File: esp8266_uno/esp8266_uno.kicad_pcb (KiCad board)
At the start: 2 copper layers, 68.5 x 53.5 mm, 126 parts, among them J1 Barrel_Jack, P1 USB, Q1 2N2222, Q2 2N2222, SW1 RESET, U1 ESP-12, U2 AMS1117-3.3, U3 CH340G, U4 ESP-13-WROOM-02, X1 12MHz

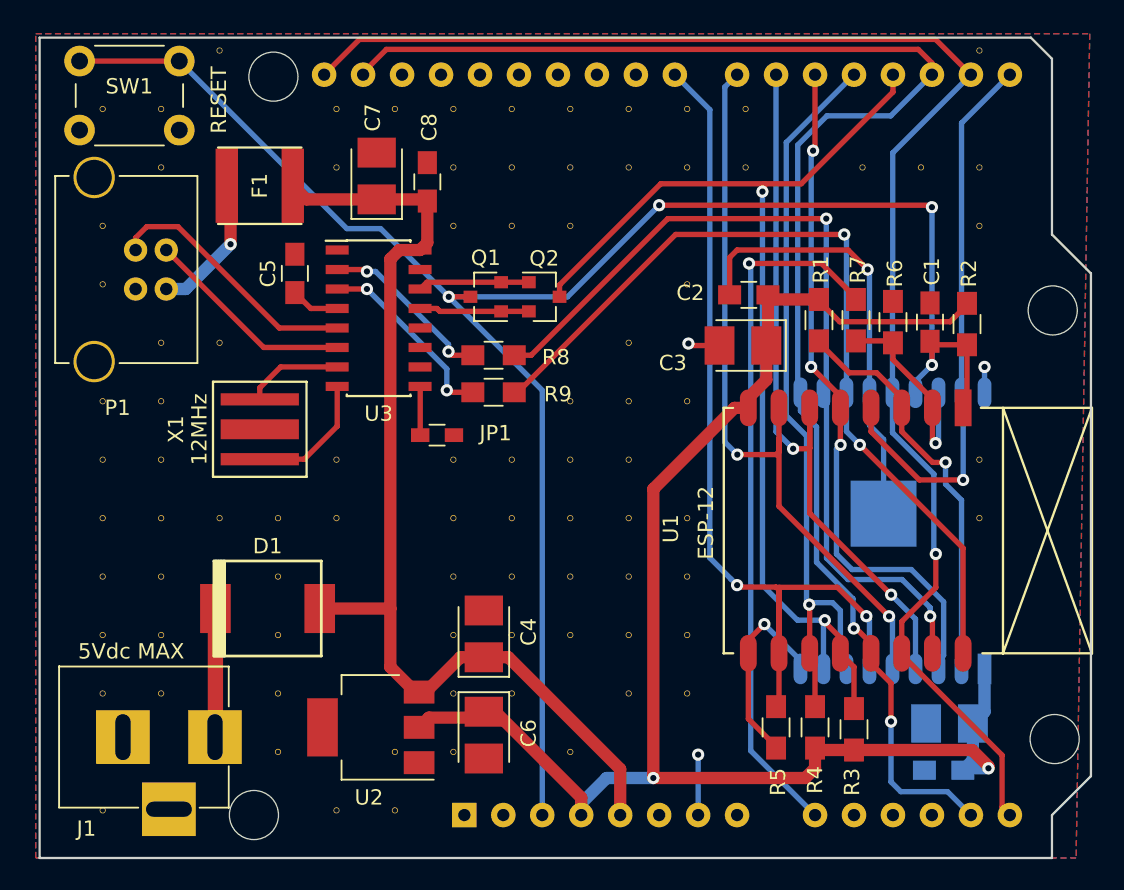
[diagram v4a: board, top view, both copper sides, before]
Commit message: added esp8266 in arduino uno format - hw design final touches
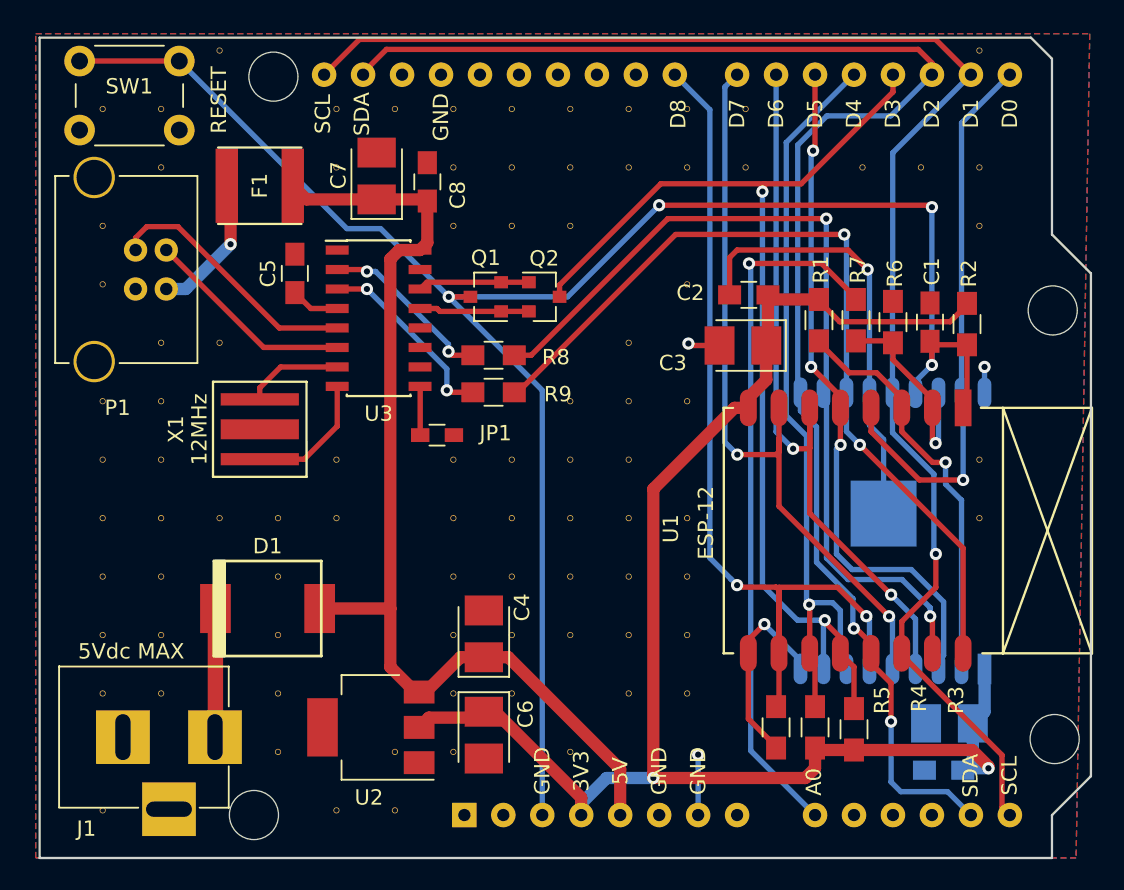
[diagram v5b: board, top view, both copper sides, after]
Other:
- board text added: "3V3"
- board text added: "5V"
- board text added: "A0"
- board text added: "D0"
- board text added: "D1"
- board text added: "D2"
- board text added: "D3"
- board text added: "D4"
- board text added: "D5"
- board text added: "D6"
- board text added: "D7"
- board text added: "D8"
- board text added: "GND"
- board text added: "SCL"
- board text added: "SDA"
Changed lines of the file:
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@@
   (general
     (thickness 1.6)
-    (drawings 56)
+    (drawings 96)
     (tracks 376)
     (zones 0)
@@
     (tags "capacitor 0805")
     (attr smd)
-    (fp_text reference C8 (at -3.556 -0.127 270) (layer F.SilkS)
+    (fp_text reference C8 (at 0.8636 -1.9812 270) (layer F.SilkS)
       (effects (font (size 1 1) (thickness 0.15)))
     )
@@
     (tags "resistor 0805")
     (attr smd)
-    (fp_text reference R3 (at 3.429 0.127 270) (layer F.SilkS)
+    (fp_text reference R3 (at -1.905 -6.6548 270) (layer F.SilkS)
       (effects (font (size 1 1) (thickness 0.15)))
     )
@@
     (tags "resistor 0805")
     (attr smd)
-    (fp_text reference R4 (at 3.429 0 270) (layer F.SilkS)
+    (fp_text reference R4 (at -1.905 -6.7818 270) (layer F.SilkS)
       (effects (font (size 1 1) (thickness 0.15)))
     )
@@
     (tags "resistor 0805")
     (attr smd)
-    (fp_text reference R5 (at 3.556 -0.127 270) (layer F.SilkS)
+    (fp_text reference R5 (at -1.778 -6.9088 270) (layer F.SilkS)
       (effects (font (size 1 1) (thickness 0.15)))
     )
@@
     (tags "capacitor tantalum smd")
     (attr smd)
-    (fp_text reference C4 (at 0.127 2.921 90) (layer F.SilkS)
+    (fp_text reference C4 (at 1.7272 2.4892 90) (layer F.SilkS)
       (effects (font (size 1 1) (thickness 0.15)))
     )
@@
     (tags "capacitor tantalum smd")
     (attr smd)
-    (fp_text reference C6 (at -0.127 -2.921 270) (layer F.SilkS)
+    (fp_text reference C6 (at -1.3716 -2.7178 270) (layer F.SilkS)
       (effects (font (size 1 1) (thickness 0.15)))
     )
@@
     (tags "capacitor tantalum smd")
     (attr smd)
-    (fp_text reference C7 (at 3.81 -0.254 90) (layer F.SilkS)
+    (fp_text reference C7 (at 0.0508 -2.4892 90) (layer F.SilkS)
       (effects (font (size 1 1) (thickness 0.15)))
     )
@@
       (net 3 GND) (clearance 0.3) (zone_connect 2))
   )
+  (gr_text SDA (at 132.1308 85.0392 90) (layer B.SilkS)
+    (effects (font (size 1 1) (thickness 0.15)) (justify mirror))
+  )
+  (gr_text GND (at 137.287 84.836 90) (layer B.SilkS)
+    (effects (font (size 1 1) (thickness 0.15)) (justify mirror))
+  )
+  (gr_text SCL (at 129.5908 85.0392 90) (layer B.SilkS)
+    (effects (font (size 1 1) (thickness 0.15)) (justify mirror))
+  )
+  (gr_text D4 (at 164.211 84.7598 90) (layer B.SilkS)
+    (effects (font (size 1 1) (thickness 0.15)) (justify mirror))
+  )
+  (gr_text D1 (at 171.831 84.7598 90) (layer B.SilkS)
+    (effects (font (size 1 1) (thickness 0.15)) (justify mirror))
+  )
+  (gr_text D0 (at 174.371 84.7598 90) (layer B.SilkS)
+    (effects (font (size 1 1) (thickness 0.15)) (justify mirror))
+  )
+  (gr_text D8 (at 152.7556 84.7344 90) (layer B.SilkS)
+    (effects (font (size 1 1) (thickness 0.15)) (justify mirror))
+  )
+  (gr_text D7 (at 156.591 84.7598 90) (layer B.SilkS)
+    (effects (font (size 1 1) (thickness 0.15)) (justify mirror))
+  )
+  (gr_text D6 (at 159.131 84.7598 90) (layer B.SilkS)
+    (effects (font (size 1 1) (thickness 0.15)) (justify mirror))
+  )
+  (gr_text D2 (at 169.291 84.7598 90) (layer B.SilkS)
+    (effects (font (size 1 1) (thickness 0.15)) (justify mirror))
+  )
+  (gr_text D3 (at 166.751 84.7598 90) (layer B.SilkS)
+    (effects (font (size 1 1) (thickness 0.15)) (justify mirror))
+  )
+  (gr_text D5 (at 161.671 84.7598 90) (layer B.SilkS)
+    (effects (font (size 1 1) (thickness 0.15)) (justify mirror))
+  )
+  (gr_text SCL (at 175.3616 127.9652 90) (layer B.SilkS)
+    (effects (font (size 1 1) (thickness 0.15)) (justify mirror))
+  )
+  (gr_text SDA (at 173.2026 127.9398 90) (layer B.SilkS)
+    (effects (font (size 1 1) (thickness 0.15)) (justify mirror))
+  )
+  (gr_text A0 (at 161.6202 128.2446 90) (layer B.SilkS)
+    (effects (font (size 1 1) (thickness 0.15)) (justify mirror))
+  )
+  (gr_text GND (at 143.891 127.635 90) (layer B.SilkS)
+    (effects (font (size 1 1) (thickness 0.15)) (justify mirror))
+  )
+  (gr_text 3V3 (at 146.431 127.635 90) (layer B.SilkS)
+    (effects (font (size 1 1) (thickness 0.15)) (justify mirror))
+  )
+  (gr_text GND (at 154.051 127.635 90) (layer B.SilkS)
+    (effects (font (size 1 1) (thickness 0.15)) (justify mirror))
+  )
+  (gr_text GND (at 151.511 127.635 90) (layer B.SilkS)
+    (effects (font (size 1 1) (thickness 0.15)) (justify mirror))
+  )
+  (gr_text 5V (at 148.971 127.635 90) (layer B.SilkS)
+    (effects (font (size 1 1) (thickness 0.15)) (justify mirror))
+  )
+  (gr_text SDA (at 132.1308 84.7344 90) (layer F.SilkS)
+    (effects (font (size 1 1) (thickness 0.15)))
+  )
+  (gr_text SCL (at 129.5908 84.7344 90) (layer F.SilkS)
+    (effects (font (size 1 1) (thickness 0.15)))
+  )
+  (gr_text GND (at 137.287 84.9376 90) (layer F.SilkS)
+    (effects (font (size 1 1) (thickness 0.15)))
+  )
+  (gr_text GND (at 154.051 127.5588 90) (layer F.SilkS)
+    (effects (font (size 1 1) (thickness 0.15)))
+  )
+  (gr_text GND (at 151.511 127.5588 90) (layer F.SilkS)
+    (effects (font (size 1 1) (thickness 0.15)))
+  )
+  (gr_text 5V (at 148.971 127.5588 90) (layer F.SilkS)
+    (effects (font (size 1 1) (thickness 0.15)))
+  )
+  (gr_text 3V3 (at 146.431 127.5588 90) (layer F.SilkS)
+    (effects (font (size 1 1) (thickness 0.15)))
+  )
+  (gr_text GND (at 143.891 127.5588 90) (layer F.SilkS)
+    (effects (font (size 1 1) (thickness 0.15)))
+  )
+  (gr_text A0 (at 161.5948 128.27 90) (layer F.SilkS)
+    (effects (font (size 1 1) (thickness 0.15)))
+  )
+  (gr_text SCL (at 174.3456 127.8636 90) (layer F.SilkS)
+    (effects (font (size 1 1) (thickness 0.15)))
+  )
+  (gr_text SDA (at 171.8056 127.8636 90) (layer F.SilkS)
+    (effects (font (size 1 1) (thickness 0.15)))
+  )
+  (gr_text D8 (at 152.7556 84.7344 90) (layer F.SilkS)
+    (effects (font (size 1 1) (thickness 0.15)))
+  )
+  (gr_text D0 (at 174.371 84.709 90) (layer F.SilkS)
+    (effects (font (size 1 1) (thickness 0.15)))
+  )
+  (gr_text D1 (at 171.831 84.709 90) (layer F.SilkS)
+    (effects (font (size 1 1) (thickness 0.15)))
+  )
+  (gr_text D2 (at 169.291 84.709 90) (layer F.SilkS)
+    (effects (font (size 1 1) (thickness 0.15)))
+  )
+  (gr_text D3 (at 166.751 84.709 90) (layer F.SilkS)
+    (effects (font (size 1 1) (thickness 0.15)))
+  )
+  (gr_text D4 (at 164.211 84.709 90) (layer F.SilkS)
+    (effects (font (size 1 1) (thickness 0.15)))
+  )
+  (gr_text D5 (at 161.671 84.709 90) (layer F.SilkS)
+    (effects (font (size 1 1) (thickness 0.15)))
+  )
+  (gr_text D6 (at 159.131 84.709 90) (layer F.SilkS)
+    (effects (font (size 1 1) (thickness 0.15)))
+  )
+  (gr_text D7 (at 156.591 84.709 90) (layer F.SilkS)
+    (effects (font (size 1 1) (thickness 0.15)))
+  )
   (gr_circle (center 140.111 82.296) (end 140.365 82.296) (layer Dwgs.User) (width 0.2))
